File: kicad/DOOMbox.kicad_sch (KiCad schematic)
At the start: 32 parts, among them J1 DE15_Socket_HighDensity, J2 AudioJack3, SW1 SW_SPST, SW2 SW_Push, U1 RPi Pico 2, U2 MCP23S08, U3 AP7381-50SA-7

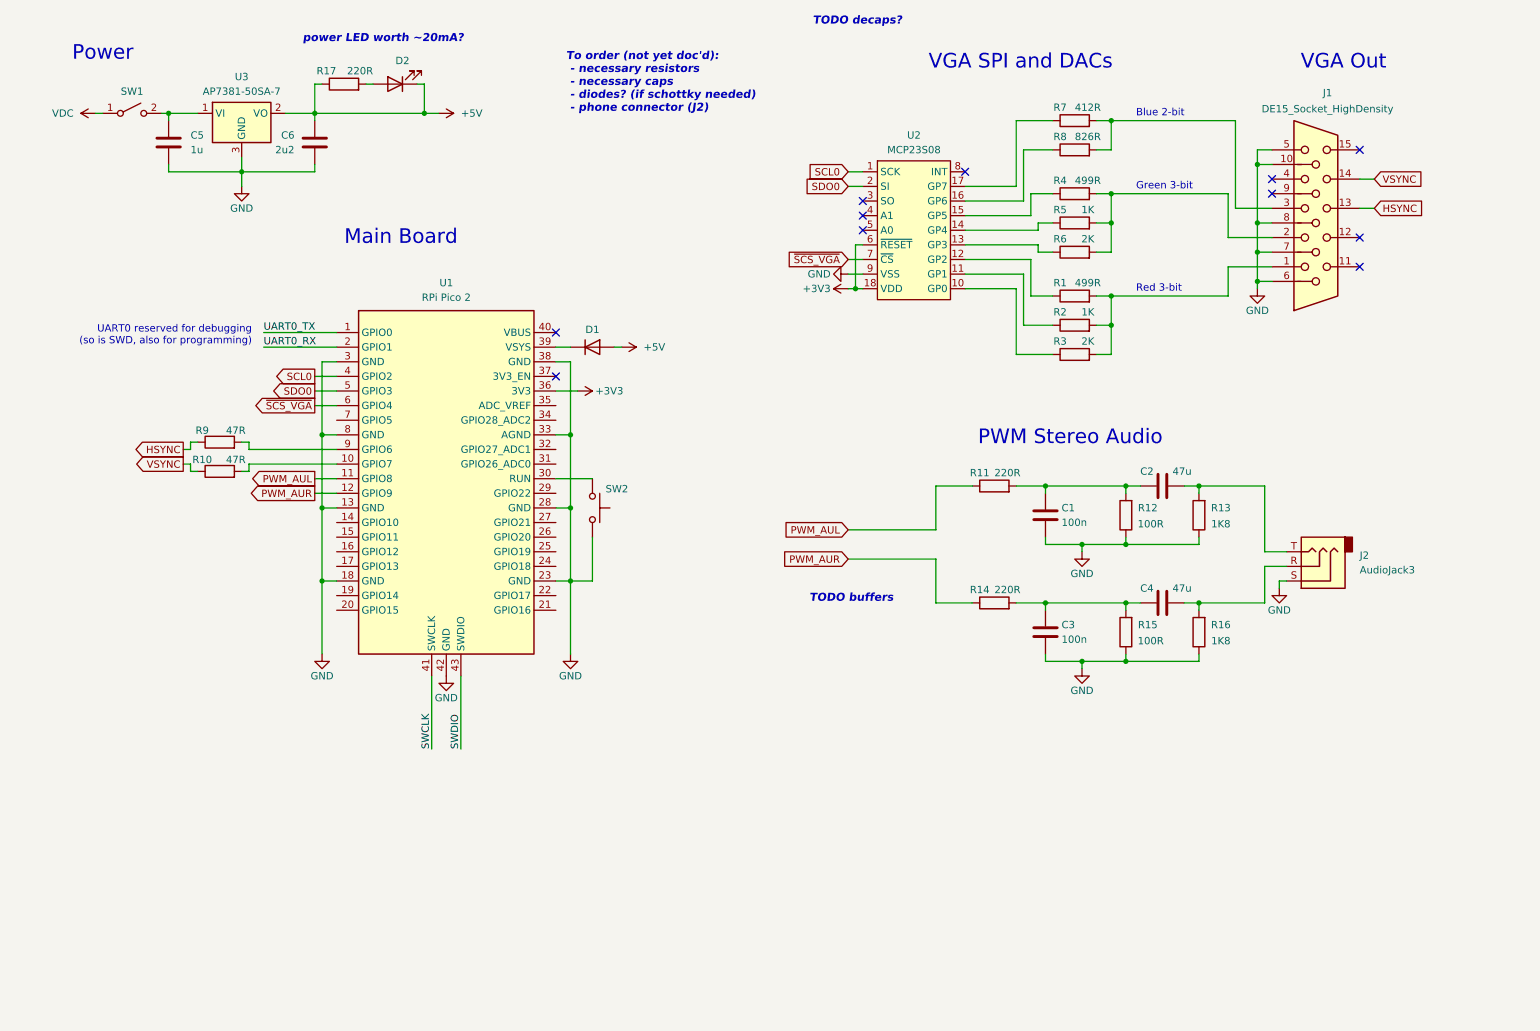
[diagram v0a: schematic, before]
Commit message: Add design for audio output w/ quad opamp + reorganise schematic
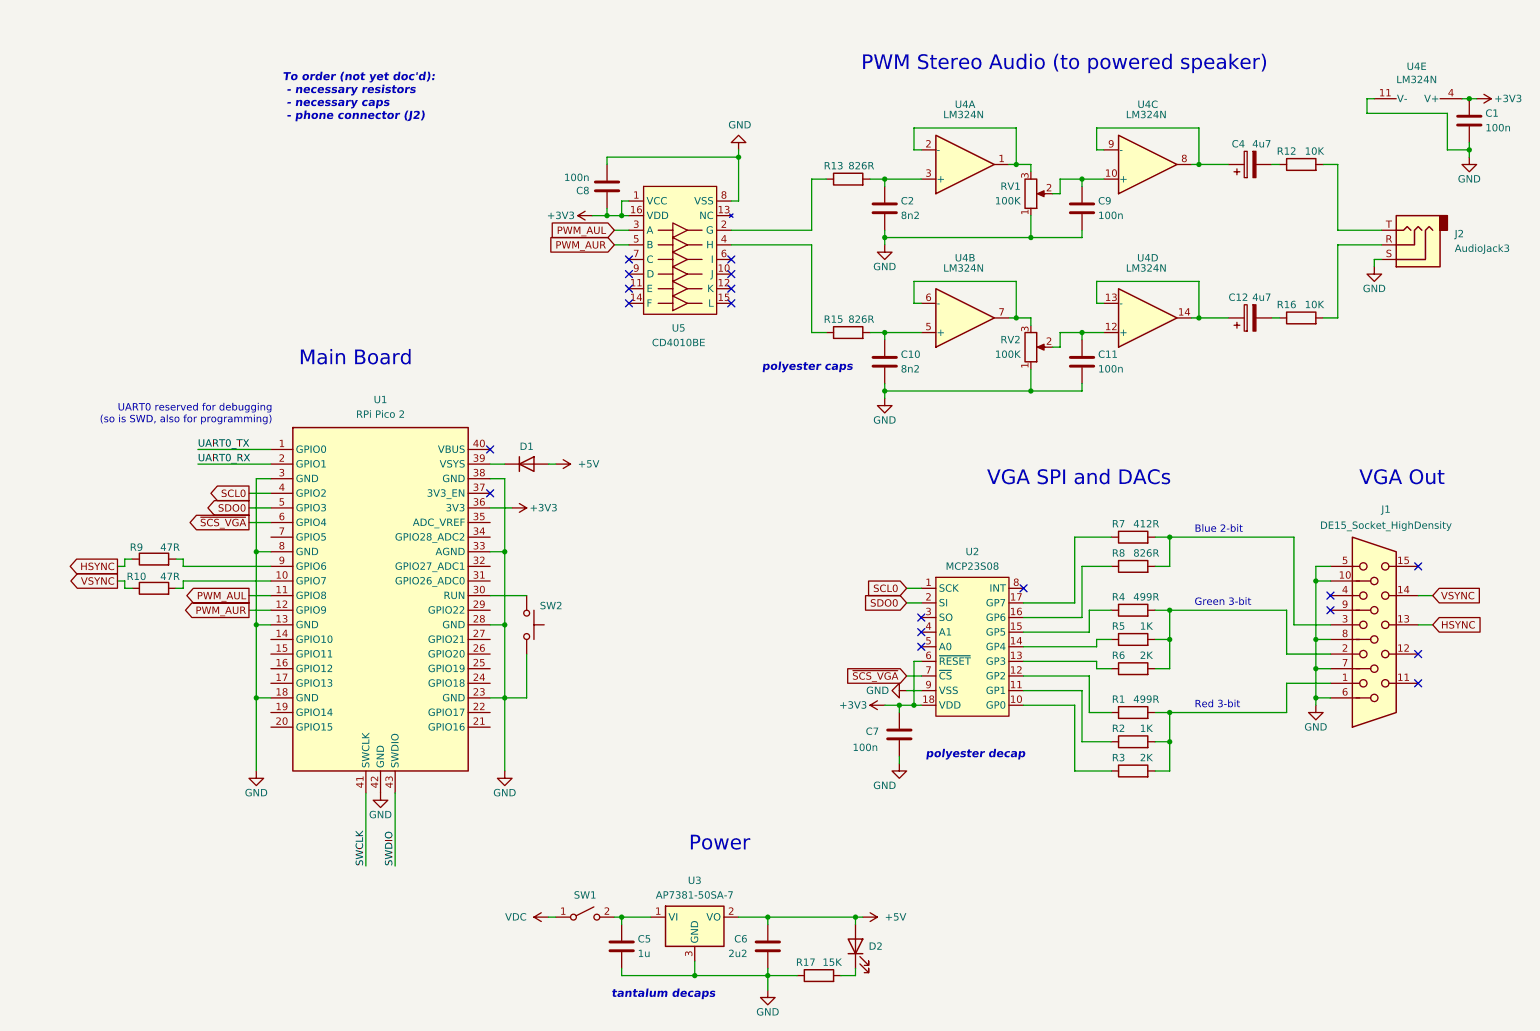
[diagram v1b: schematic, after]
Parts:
- removed C3: 100n, symbol Device:C
- removed C4: 47u, symbol Device:C
- removed R11, R14: 220R, symbol Device:R
- added C10: 8n2, symbol Device:C
- added C11, C7, C8, C9: 100n, symbol Device:C
- added C12, C4: 4u7, symbol Device:C_Polarized
- added RV1, RV2: 100K, symbol Device:R_Potentiometer
- added U4: LM324N, symbol Amplifier_Operational:LM324
- added U5: CD4010BE, symbol CD40xxBx:CD4010BE
- C2: value 47u -> 8n2
- R12: value 100R -> 10K
- R13: value 1K8 -> 826R
- R15: value 100R -> 826R
- R16: value 1K8 -> 10K
- R17: value 220R -> 15K
- U2: footprint (none) -> MCU_Microchip_MCP:DIP794W56P254L2286H533Q18N
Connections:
- net +3V3: now also C1.1, C7.1, C8.1, U4.4 (V+), U5.1 (VCC), U5.16 (VDD)
- net +5V: now also D2.2 (A); no longer D2.1 (K), R17.1
- net GND: now also C2.2, R17.1, C10.2, C11.2, C7.2, C8.2, C9.2, RV1.1, RV2.1, U4.11 (V-), U5.8 (VSS); no longer R12.1, R13.1, R15.1, R16.1
- net PWM_AUL: now also U5.3 (A)
- net PWM_AUR: now also U5.5 (B)
- net at R15.2: now also C10.1, U4.5 (+)
- net at R17.2: now also D2.1 (K); no longer D2.2 (A)
- new net: C9.1, RV1.2, U4.10 (+)
- new net: C4.1, U4.8, U4.9 (-)
- new net: C11.1, RV2.2, U4.12 (+)
- new net: RV2.3, U4.6 (-), U4.7
- new net: C4.2, R12.1
- new net: J2.T, R12.2
- new net: C2.1, R13.2, U4.3 (+)
- new net: R13.1, U5.2 (G)
- new net: R15.1, U5.4 (H)
- new net: C12.1, U4.13 (-), U4.14
- new net: C12.2, R16.1
- new net: RV1.3, U4.1, U4.2 (-)
- no-connect marks 11 -> 19
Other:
- note added: "PWM Stereo Audio (to powered speaker)"
- note added: "To order (not yet doc'd): - necessary resistors - necessary caps - phone connector (J2)"
- note added: "polyester caps"
- note added: "polyester decap"
- note added: "tantalum decaps"
- note removed: "PWM Stereo Audio"
- note removed: "TODO buffers"
- note removed: "TODO decaps?"
- note removed: "To order (not yet doc'd): - necessary resistors - necessary caps - diodes? (if schottky needed) - phone connector (J2)"
- note removed: "power LED worth ~20mA?"
- moved on the sheet: C5, C6, D1, J1, J2, R1, R10, R2, R3, R4, R5, R6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

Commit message: Remove BOM sheet
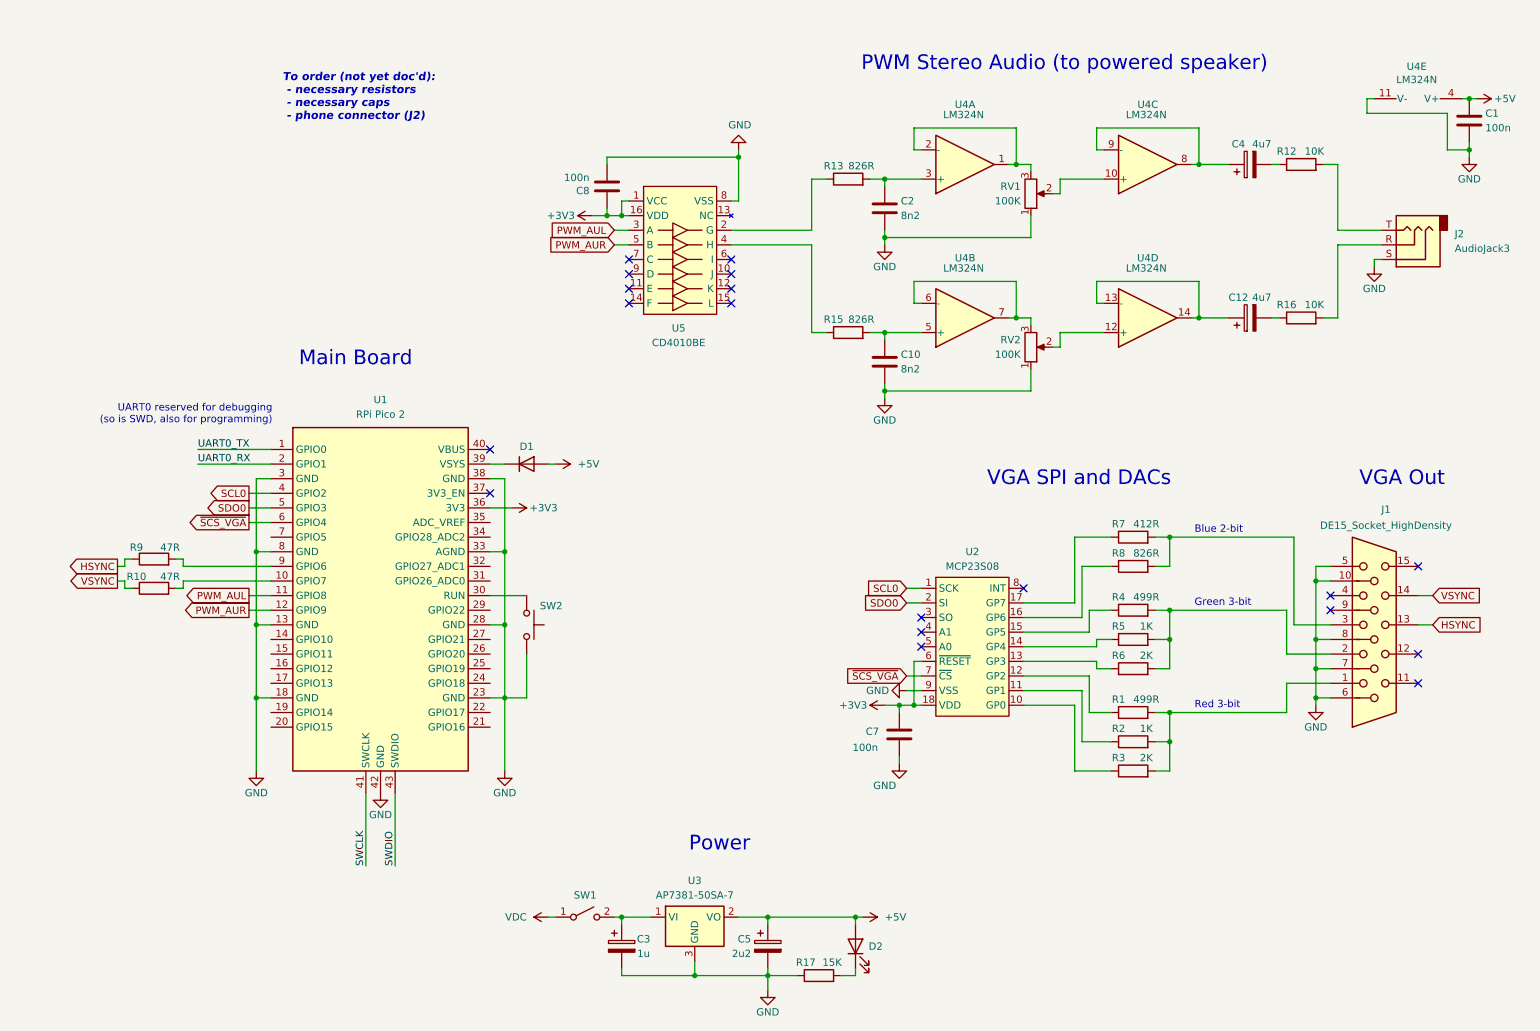
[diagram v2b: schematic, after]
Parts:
- removed C11, C9: 100n, symbol Device:C
- removed C5: 1u, symbol Device:C
- removed C6: 2u2, symbol Device:C
- added C3: 1u, symbol Device:C_Polarized
- added C5: 2u2, symbol Device:C_Polarized
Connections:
- net +3V3: no longer C1.1, U4.4 (V+)
- net +5V: now also C1.1, U4.4 (V+), C5.1
- net GND: now also C3.2, C5.2
- net at SW1.2 (B), U3.1 (VI): now also C3.1
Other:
- note removed: "polyester caps"
- note removed: "polyester decap"
- note removed: "tantalum decaps"

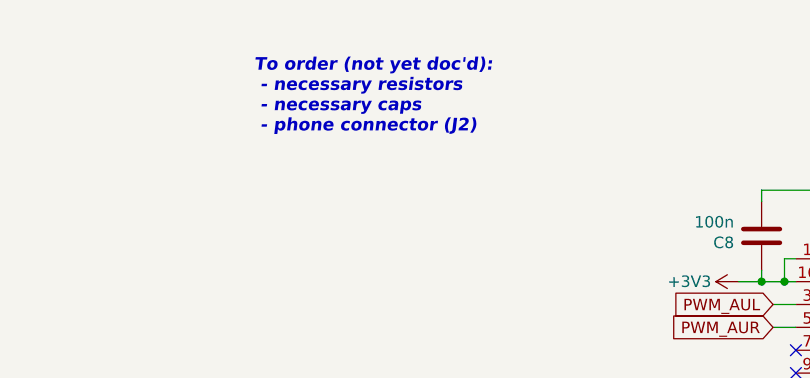
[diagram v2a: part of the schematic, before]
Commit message: Remove outdated to-order list
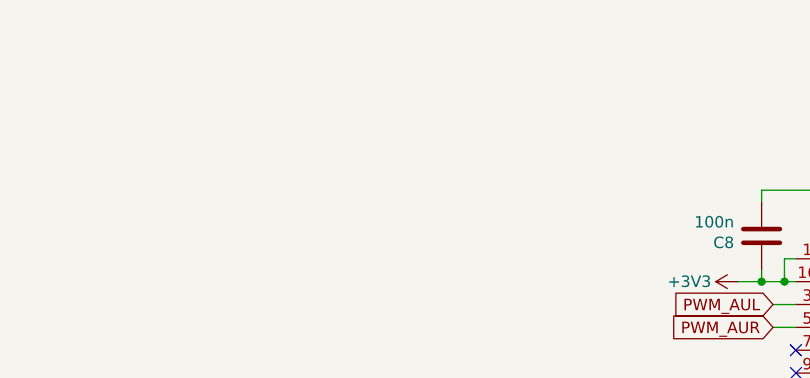
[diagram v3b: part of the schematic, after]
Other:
- note removed: "To order (not yet doc'd): - necessary resistors - necessary caps - phone connector (J2)"
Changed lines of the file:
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@@
-		)
-	)
-	(text "To order (not yet doc'd):\n - necessary resistors\n - necessary caps\n - phone connector (J2)"
-		(exclude_from_sim no)
-		(at 61.722 30.226 0)
-		(effects
-			(font
-				(size 1.397 1.397)
-				(thickness 0.254)
-				(bold yes)
-				(italic yes)
-				(color 255 0 0 1)
-			)
-			(justify left)
 		)
 	)

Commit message: README update
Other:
- note added: "Video SPI and DACs"
- note removed: "VGA SPI and DACs"
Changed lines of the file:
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@@
 		(company "Jack Bennett")
 	)
-	(text "VGA SPI and DACs"
+	(text "Video SPI and DACs"
 		(exclude_from_sim no)
 		(at 200.152 96.52 0)
